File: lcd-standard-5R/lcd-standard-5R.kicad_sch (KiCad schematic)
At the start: 50 parts, among them J1 SWD, J2 Conn_01x40_MountingPin, J3 Micro_SD_Card_Det1, J5 Conn_01x06_MountingPin, SW1 BOOT0, SW2 RST, U1 siplex-som-s16, U2 TPS61169

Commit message: Added Serial, Buzzer, AUX-IO, POWER switch, XPT2046, TAG-connect, EEPROM
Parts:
- removed C7: 100n, Capacitor_SMD:C_0603_1608Metric, symbol Device:C_Small
- added BZ1: MLT-9650, SMD-Buzzer:active-MLT-9650, symbol Device:Buzzer
- added C11, C19: 10u, Capacitor_SMD:C_0805_2012Metric, symbol Device:C
- added C13, C14, C15, C16, C17, C20: 100n, Capacitor_SMD:C_0603_1608Metric, symbol Device:C_Small
- added C18: 100n, Capacitor_SMD:C_0402_1005Metric, symbol Device:C_Small
- added C21: 22uF, Capacitor_Tantalum_SMD:CP_EIA-3528-12_Kemet-T, symbol Device:C_Polarized
- added C22: 1u, Capacitor_SMD:C_0603_1608Metric, symbol Device:C
- added C23: 100n, Capacitor_SMD:C_0603_1608Metric, symbol Device:C
- added D10, D11: BAT54S, Package_TO_SOT_SMD:SOT-23, symbol Diode:BAT54S
- added D12: MBR0540, Diode_SMD:D_SOD-123, symbol Diode:MBR0540
- added D6, D7, D8, D9: MMSZ5226BT1G, Diode_SMD:D_SOD-123, symbol Device:D_Zener
- added J6: Serial, S4B-XH-SM4-TB_LF__SN:S4BXHSM4TBLFSN, symbol Connector_Generic_MountingPin:Conn_01x04_MountingPin
- added J7: Conn_ARM_JTAG_SWD_10, Connector:Tag-Connect_TC2050-IDC-NL_2x05_P1.27mm_Vertical, symbol Connector:Conn_ARM_JTAG_SWD_10
- added J8: Conn_01x12_MountingPin, Connector_JST:JST_SH_SM12B-SRSS-TB_1x12-1MP_P1.00mm_Horizontal, symbol Connector_Generic_MountingPin:Conn_01x12_MountingPin
- added JP1, JP2, JP3: JMP, Jumper:SolderJumper-2_P1.3mm_Open_RoundedPad1.0x1.5mm, symbol Jumper:SolderJumper_2_Open
- added Q1: DMG2301L, Package_TO_SOT_SMD:SOT-23, symbol Transistor_FET:DMG2301L
- added Q2: MMBT3904, Package_TO_SOT_SMD:SOT-23, symbol Transistor_BJT:MMBT3904
- added R17, R18, R19, R20, R21: 2K2, Resistor_SMD:R_0402_1005Metric, symbol Device:R_Small
- added R22, R25: 10K, Resistor_SMD:R_0402_1005Metric, symbol Device:R_Small
- added R23: 0, Resistor_SMD:R_1206_3216Metric, symbol Device:R
- added R24: 1K, Resistor_SMD:R_0402_1005Metric, symbol Device:R_Small
- added TP1, TP2, TP3, TP4, TP5, TP6, TP7: TestPoint, TestPoint:TestPoint_Pad_D1.0mm, symbol Connector:TestPoint
- added U3: XPT2046TS, Package_SO:TSSOP-16_4.4x5mm_P0.65mm, symbol Driver_Display:XPT2046TS
- added U4: CAT24C256, Package_SO:SOIC-8_3.9x4.9mm_P1.27mm, symbol Memory_EEPROM:CAT24C256
- added U5: AMS1117-3.3, Package_TO_SOT_SMD:SOT-223-3_TabPin2, symbol Regulator_Linear:AMS1117-3.3
- C1: footprint Capacitor_SMD:C_0603_1608Metric -> Capacitor_SMD:C_1206_3216Metric
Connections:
- net +3V3: now also C11.1, C13.1, C18.1, C21.1, C22.1, C23.1, D10.2 (K), D11.2 (K), JP1.2 (B), JP2.2 (B), JP3.2 (B), R17.1, R18.1, TP7.1, U3.1 (VCC), U3.10 (IOVDD), U3.9 (VREF), U4.8 (VCC), U5.2 (VO)
- net GND: now also R1.2, C11.2, C13.2, C14.2, C15.2, C16.2, C17.2, C18.2, C19.2, C20.2, C21.2, C22.2, C23.2, D10.1 (A), D11.1 (A), D6.2 (A), D7.2 (A), D8.2 (A), D9.2 (A), J6.4 (Pin_4), J6.MP (MountPin), J7.3 (GND), J7.5 (GND), J8.MP (MountPin), Q2.2 (E), R19.2, R20.2, R21.2, R22.2, R25.2, TP3.1, TP5.1, U3.6 (GND), U4.4 (GND), U4.7 (WP), U5.1 (GND)
- net LCD_BLK: now also R1.1; no longer R1.2
- net LED_A: now also TP4.1
- net RESET: now also J7.10 (~{RESET})
- net SWCLK: now also J7.4 (SWCLK/TCK)
- net SWDIO: now also J7.2 (SWDIO/TMS)
- net SWO: now also J7.6 (SWO/TDO)
- net VBUS: now also Q1.3 (D), TP6.1; no longer U1.41 (VIN)
- net XL: now also C16.1, D8.1 (K), U3.4 (XN)
- net XR: now also C14.1, D6.1 (K), U3.2 (XP)
- net YD: now also C15.1, D7.1 (K), U3.3 (YP)
- net YU: now also C17.1, D9.1 (K), U3.5 (YN)
- net +5V renamed VDD
- net VDD: now also U1.41 (VIN), BZ1.1 (+), C19.1, C20.1, D12.1 (K), Q1.2 (S), R23.2, TP2.1, U5.3 (VI); no longer R1.1
- new net: JP1.1 (A), R20.1, U4.3 (A2)
- new net: JP2.1 (A), R19.1, U4.2 (A1)
- new net: Q2.1 (B), R24.2, R25.1
- new net: R18.2, U4.6 (SCL)
- new net: R17.2, U4.5 (SDA)
- new net: BZ1.2 (-), Q2.3 (C)
- new net: JP3.1 (A), R21.1, U4.1 (A0)
- new net BUZZER: R24.1
- new net SERIAL_RX: D10.3 (COM), J6.3 (Pin_3)
- new net SERIAL_TX: D11.3 (COM), J6.2 (Pin_2)
- new net TP_BUSY: U3.13 (BUSY)
- new net TP_CLK: U3.16 (DCLK)
- new net TP_CS: U3.15 (~{CS})
- new net TP_IRQ: U3.11 (~{PENIRQ})
- new net TP_MISO: U3.12 (DOUT)
- new net TP_MOSI: U3.14 (DIN)
- new net VEXT: D12.2 (A), J6.1 (Pin_1), Q1.1 (G), R22.1, R23.1, TP1.1
- no-connect marks 4 -> 6
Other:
- moved on the sheet: R1

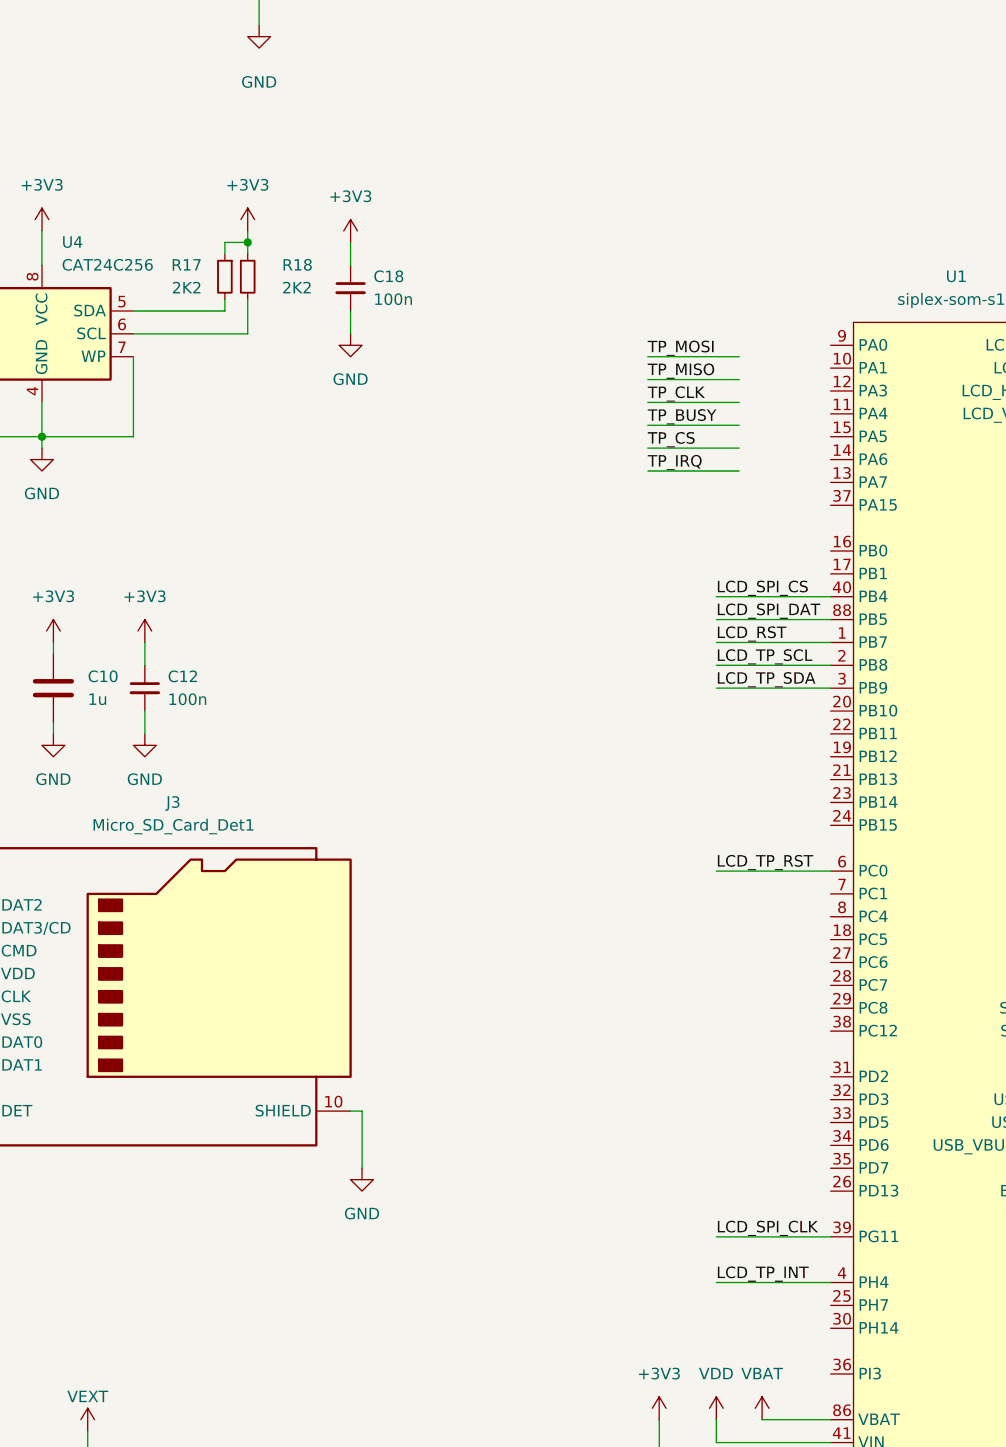
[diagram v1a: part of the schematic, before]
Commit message: LCD 5 inch, Finished SD card, Touch, Buzzer etc, LCD Bar 3.4, Adding resistor on st-link, not finished yet
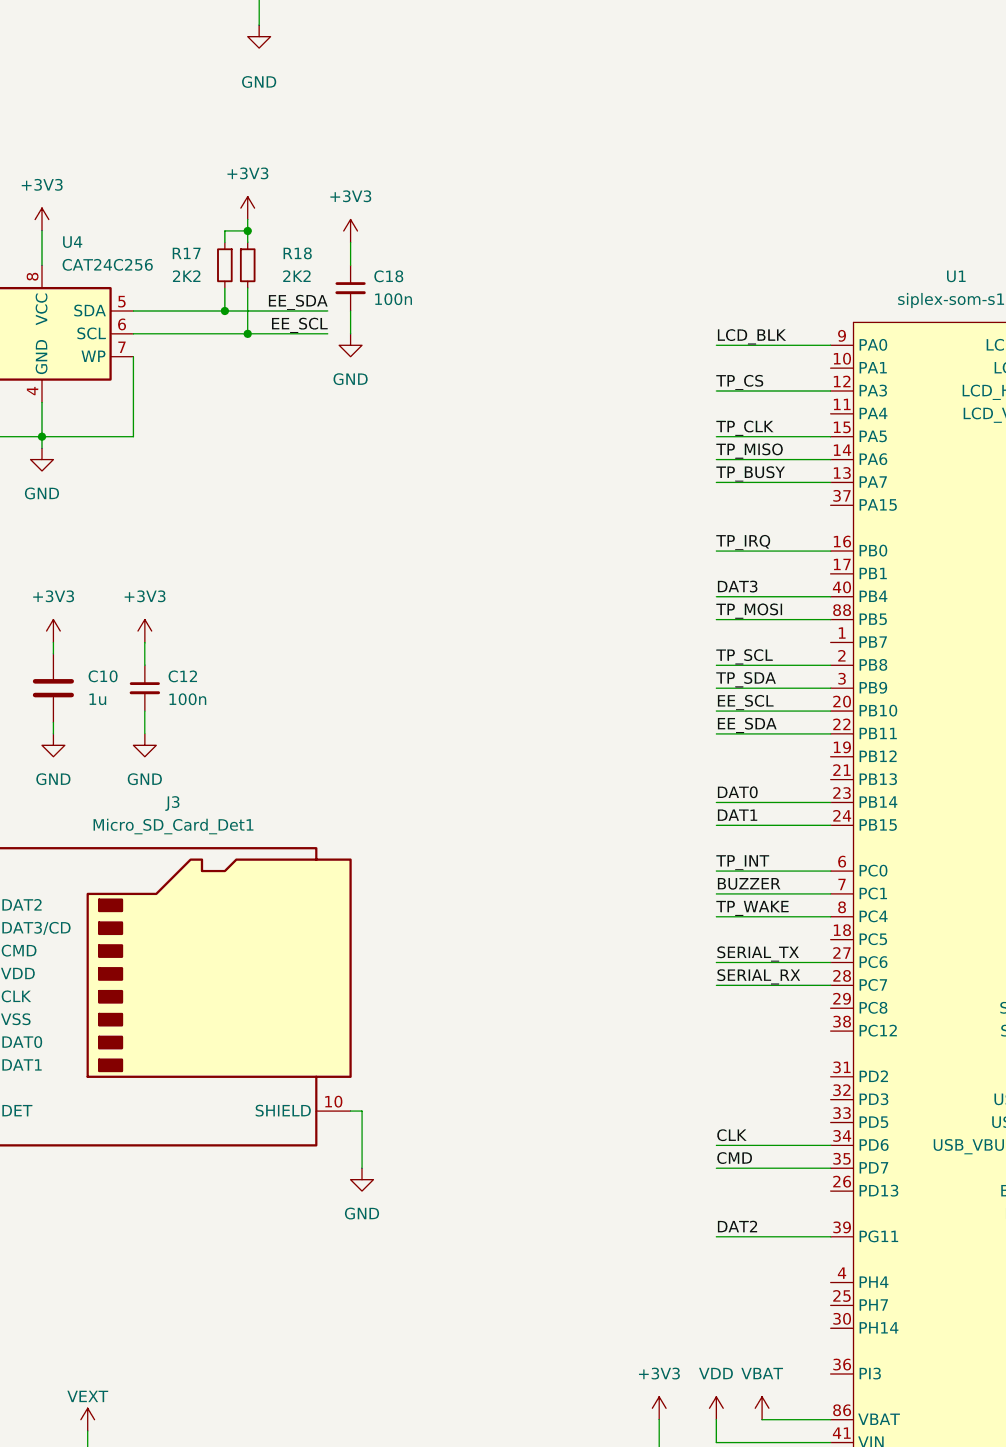
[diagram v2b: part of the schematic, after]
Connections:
- net LCD_SPI_CLK is gone; now on net DAT2: U1.39 (PG11)
- net LCD_SPI_CS is gone; now on net DAT3: U1.40 (PB4)
- net LCD_SPI_DAT is gone; now on net TP_MOSI: U1.88 (PB5)
- net LCD_TP_RST is gone; now on net TP_INT: U1.6 (PC0)
- net LCD_TP_SCL is gone; now on net TP_SCL: U1.2 (PB8)
- net LCD_TP_SDA is gone; now on net TP_SDA: U1.3 (PB9)
- net BUZZER: now also U1.7 (PC1)
- net CLK: now also U1.34 (PD6)
- net CMD: now also U1.35 (PD7)
- net DAT0: now also U1.23 (PB14)
- net DAT1: now also U1.24 (PB15)
- net LCD_BLK: now also U1.9 (PA0)
- net LCD_RST: no longer U1.1 (PB7)
- net SERIAL_RX: now also U1.28 (PC7)
- net SERIAL_TX: now also U1.27 (PC6)
- net TP_BUSY: now also U1.13 (PA7)
- net TP_CLK: now also U1.15 (PA5)
- net TP_CS: now also U1.12 (PA3)
- net TP_IRQ: now also U1.16 (PB0)
- net TP_MISO: now also U1.14 (PA6)
- net TP_WAKE: now also U1.8 (PC4)
- net EE_SCL: now reaches R18.2, U4.6 (SCL)
- net EE_SCL: now also U1.20 (PB10)
- net EE_SDA: now reaches R17.2, U4.5 (SDA)
- net EE_SDA: now also U1.22 (PB11)
- net LCD_TP_INT: no longer names the net of U1.4 (PH4)
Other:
- moved on the sheet: R17, R18

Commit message: Adding MAX98357 I2S mono Amplifier
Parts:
- removed J8: Conn_01x12_MountingPin, Connector_JST:JST_SH_SM12B-SRSS-TB_1x12-1MP_P1.00mm_Horizontal, symbol Connector_Generic_MountingPin:Conn_01x12_MountingPin
- removed U1: siplex-som-s16, siplex:siplex-som-s16, symbol siplex-som:siplex-som-s16
- added C7: 10u, Capacitor_SMD:C_0805_2012Metric, symbol Device:C
- added J8: Conn_01x02_MountingPin, Connector_Hirose:Hirose_DF3EA-02P-2H_1x02-1MP_P2.00mm_Horizontal, symbol Connector_Generic_MountingPin:Conn_01x02_MountingPin
- added J9: Conn_01x10_MountingPin, Connector_JST:JST_SHL_SM10B-SHLS-TF_1x10-1MP_P1.00mm_Horizontal, symbol Connector_Generic_MountingPin:Conn_01x10_MountingPin
- added Q3, Q4: MMBT3904, Package_TO_SOT_SMD:SOT-23, symbol Transistor_BJT:MMBT3904
- added R26, R28: 1K, Resistor_SMD:R_0402_1005Metric, symbol Device:R_Small
- added R27, R29, R30, R31: 10K, Resistor_SMD:R_0402_1005Metric, symbol Device:R_Small
- added R32: 100K, Resistor_SMD:R_0402_1005Metric, symbol Device:R_Small
- added R33: 1M, Resistor_SMD:R_0402_1005Metric, symbol Device:R_Small
- added U1: MAX98357A, Package_DFN_QFN:TQFN-16-1EP_3x3mm_P0.5mm_EP1.23x1.23mm, symbol Audio:MAX98357A
- added U6: siplex-som-s16, siplex:siplex-som-s16, symbol siplex-som:siplex-som-s16
- J7: now left out of the parts list
- R2: value 6.8R -> 4.7R
- RN1, RN2, RN3, RN4, RN5, RN6, RN7: value 22 -> 100
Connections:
- net +3V3: now also R11.2, R3.2, R30.1, R31.1
- net B0: now also U6.70 (B0)
- net B1: now also U6.71 (B1)
- net B2: now also U6.72 (B2)
- net B3: now also U6.73 (B3)
- net B4: now also U6.74 (B4)
- net B5: now also U6.75 (B5)
- net B6: now also U6.76 (B6)
- net B7: now also U6.77 (B7)
- net BOOT0: now also U6.84 (BOOT0)
- net BUZZER: now also U6.7 (PC1)
- net CLK: now also U6.34 (PD6)
- net CMD: now also U6.35 (PD7)
- net DAT0: now also U6.23 (PB14)
- net DAT1: now also U6.24 (PB15)
- net DAT2: now also U6.39 (PG11)
- net DAT3: now also U6.40 (PB4)
- net EE_SCL: now also U6.20 (PB10)
- net EE_SDA: now also U6.22 (PB11)
- net G0: now also U6.62 (G0)
- net G1: now also U6.63 (G1)
- net G2: now also U6.64 (G2)
- net G3: now also U6.65 (G3)
- net G4: now also U6.66 (G4)
- net G5: now also U6.67 (G5)
- net G6: now also U6.68 (G6)
- net G7: now also U6.69 (G7)
- net GND: now also C7.2, J8.MP (MountPin), J9.1 (Pin_1), J9.10 (Pin_10), J9.MP (MountPin), Q3.2 (E), Q4.2 (E), R27.2, R29.2, R32.2, U1.11 (GND), U1.15 (GND), U1.17 (PAD), U1.3 (GND), U6.43 (GND), U6.44 (GND), U6.47 (GND), U6.5 (GND), U6.50 (GND), U6.53 (GND), U6.78 (GND), U6.80 (GND), U6.87 (GND); no longer D3.1 (K), D4.1 (K)
- net LCD_BLK: now also U6.9 (PA0)
- net LCD_RST: now also U6.1 (PB7)
- net LED0: now also R26.1, U6.17 (PB1); no longer R3.1
- net LED1: now also R28.1, U6.11 (PA4); no longer R11.1
- net R1: now also U6.55 (R1)
- net R2: now also U6.56 (R2)
- net R3: now also U6.57 (R3)
- net R4: now also U6.58 (R4)
- net R5: now also U6.59 (R5)
- net R6: now also U6.60 (R6)
- net R7: now also U6.61 (R7)
- net RESET: now also U6.85 (RESET)
- net SERIAL_RX: now also U6.28 (PC7)
- net SERIAL_TX: now also U6.27 (PC6)
- net SWCLK: now also U6.46 (SWCLK)
- net SWDIO: now also U6.45 (SWDIO)
- net SWO: now also U6.52 (SWO)
- net TP_BUSY: now also U6.13 (PA7)
- net TP_CLK: now also U6.15 (PA5)
- net TP_CS: now also R31.2, U6.12 (PA3)
- net TP_INT: now also U6.6 (PC0)
- net TP_IRQ: now also R30.2, U6.16 (PB0)
- net TP_MISO: now also U6.14 (PA6)
- net TP_MOSI: now also U6.88 (PB5)
- net TP_SCL: now also U6.2 (PB8)
- net TP_SDA: now also U6.3 (PB9)
- net TP_WAKE: now also U6.8 (PC4)
- net USB_DN: now also U6.48 (USB_DN)
- net USB_DP: now also U6.49 (USB_DP)
- net USB_VBUS_DET: now also U6.51 (USB_VBUS_DET)
- net VBAT: now also U6.86 (VBAT)
- net VDD: now also C7.1, U1.7 (VDD), U1.8 (VDD), U6.41 (VIN)
- net at D4.2 (A): now also R11.1; no longer R11.2
- net at RN1.8 (R1.2): now also U6.54 (R0)
- net at D3.2 (A): now also R3.1; no longer R3.2
- net at RN4.8 (R1.2): now also U6.79 (LCD_CLK)
- net at RN4.6 (R3.2): now also U6.82 (LCD_VSYNC)
- net at RN4.7 (R2.2): now also U6.81 (LCD_HSYNC)
- net at RN4.5 (R4.2): now also U6.83 (LCD_DE)
- net VCP_RX renamed DBG_RX
- net DBG_RX: now also U6.31 (PD2)
- net VCP_TX renamed DBG_TX
- net DBG_TX: now also U6.38 (PC12)
- new net: Q4.1 (B), R28.2, R29.1
- new net: J8.1 (Pin_1), U1.9 (OUTP)
- new net: J8.2 (Pin_2), U1.10 (OUTN)
- new net: D4.1 (K), Q4.3 (C)
- new net: R33.1, U1.4 (~{SD_MODE})
- new net: Q3.1 (B), R26.2, R27.1
- new net: D3.1 (K), Q3.3 (C)
- new net GAIN_SLOT: R32.1, U1.2 (GAIN_SLOT)
- new net I2S2_CLK: U1.16 (BCLK), U6.21 (PB13)
- new net I2S2_SDO: U1.1 (DIN), U6.36 (PI3)
- new net I2S2_WS: U1.14 (LRCLK), U6.19 (PB12)
- new net IO_0: J9.9 (Pin_9), U6.37 (PA15)
- new net IO_1: J9.8 (Pin_8), U6.33 (PD5)
- new net IO_2: J9.7 (Pin_7), U6.32 (PD3)
- new net IO_3: J9.6 (Pin_6), U6.30 (PH14)
- new net IO_4: J9.5 (Pin_5), U6.29 (PC8)
- new net IO_5: J9.4 (Pin_4), U6.26 (PD13)
- new net IO_6: J9.3 (Pin_3), U6.25 (PH7)
- new net IO_7: J9.2 (Pin_2), U6.18 (PC5)
- new net ~{SD_MODE}: R33.2, U6.10 (PA1)
- no-connect marks 6 -> 7
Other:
- note added: "45mA"
- note added: "I2C1"
- note added: "I2C2"
- note added: "SDMMC2"
- note added: "SPI1"
- note added: "TIM2-CH1"
- note added: "UART5"
- note added: "USART6"
- note removed: "30mA"
- moved on the sheet: D3, D4, R11, R3, RN1, RN2, RN3, RN4, RN5, RN6, RN7

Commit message: Add LCD standard 7inch
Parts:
- J8: footprint Connector_Hirose:Hirose_DF3EA-02P-2H_1x02-1MP_P2.00mm_Horizontal -> Connector_Hirose:Hirose_DF13C_CL535-0402-2-51_1x02-1MP_P1.25mm_Vertical
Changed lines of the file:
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@@
 	(label "~{SD_MODE}"
 		(at -213.36 95.25 0)
+		(fields_autoplaced yes)
 		(effects
 			(font
@@
 	(label "GAIN_SLOT"
 		(at -196.85 97.79 0)
+		(fields_autoplaced yes)
 		(effects
 			(font
@@
 			)
 		)
-		(property "Footprint" "Connector_Hirose:Hirose_DF3EA-02P-2H_1x02-1MP_P2.00mm_Horizontal"
+		(property "Footprint" "Connector_Hirose:Hirose_DF13C_CL535-0402-2-51_1x02-1MP_P1.25mm_Vertical"
 			(at -146.05 85.09 0)
 			(effects
